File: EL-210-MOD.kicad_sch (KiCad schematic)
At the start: 2 parts, among them P1 EL-210-KEY, U1 9-ST-20

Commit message: Rough layout of the digital part.
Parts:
- added U2: STM32G0B1KET6, Package_QFP:LQFP-32_7x7mm_P0.8mm, symbol STM32G0B1KET6:STM32G0B1KET6
- added U3: MAX6934AQH+D, Package_LCC:PLCC-44, symbol MAX6934A:MAX6934AQH+D
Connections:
- net +3V3: now also U2.4 (VDD/VDDA)
- net GND: now also U2.5 (VSS/VSSA), U3.22 (GND)
- net KD3: now reaches P1.10 (D3)
- net KD3: now also U2.10 (PA3)
- net KD2: now reaches P1.11 (D2)
- net KD2: now also U2.9 (PA2)
- net KD1: now reaches P1.13 (D1)
- net KD1: now also U2.8 (PA1)
- net KD0: now reaches P1.14 (D0)
- net KD0: now also U2.7 (PA0)
- net KEY1: now reaches P1.2 (KEY1)
- net KEY1: now also U2.21 (PA10)
- net KEY2: now reaches P1.3 (KEY2)
- net KEY2: now also U2.20 (PC6)
- net KEY3: now reaches P1.4 (KEY3)
- net KEY3: now also U2.17 (PB2)
- net KD8: now reaches P1.5 (D8)
- net KD8: now also U2.16 (PB1)
- net KD7: now reaches P1.6 (D7)
- net KD7: now also U2.15 (PB0)
- net KD6: now reaches P1.7 (D6)
- net KD6: now also U2.13 (PA6)
- net KD5: now reaches P1.8 (D5)
- net KD5: now also U2.12 (PA5)
- net KD4: now reaches P1.9 (D4)
- net KD4: now also U2.11 (PA4)
- net H1: now reaches U1.1 (H1)
- net at U1.10 (D4): now also U3.34 (OUT8)
- net at U1.11 (Seg_d): now also U3.35 (OUT7)
- net at U1.12 (D3): now also U3.36 (OUT6)
- net at U1.13 (DP): now also U3.37 (OUT5)
- net at U1.14 (D2): now also U3.38 (OUT4)
- net at U1.15 (Seg_c): now also U3.39 (OUT3)
- net at U1.16 (D1): now also U3.40 (OUT2)
- net at U1.17 (Seg_b): now also U3.41 (OUT1)
- net at U1.18 (D0): now also U3.42 (OUT0)
- net H2: now reaches U1.19 (H2)
- net SEG_A: now reaches U1.2 (Seg_a)
- net SEG_A: now also U3.20 (OUT16)
- net at U1.3 (D8): now also U3.25 (OUT15)
- net at U1.4 (Seg_g): now also U3.26 (OUT14)
- net at U1.5 (D7): now also U3.27 (OUT13)
- net at U1.6 (Seg_f): now also U3.30 (OUT12)
- net at U1.7 (D6): now also U3.31 (OUT11)
- net at U1.8 (Seg_e): now also U3.32 (OUT10)
- net at U1.9 (D5): now also U3.33 (OUT9)
- new net BLANK: U2.23 (PA12_PA10), U3.21 (BLANK)
- new net EN24V: U2.32 (PB8)
- new net LOAD: U2.22 (PA11_PA9), U3.24 (LOAD)
- new net LPUART2_RX: U2.31 (PB7)
- new net LPUART2_TX: U2.30 (PB6)
- new net NRST: U2.6 (PF2-NRST)
- new net SPI1_MOSI: U2.29 (PB5), U3.43 (DIN)
- new net SPI1_SCK: U2.27 (PB3), U3.23 (CLK)
- new net SWCLK: U2.25 (PA14-BOOT0)
- new net SWDIO: U2.24 (PA13)
- new net TIM1_CH1: U2.18 (PA8)
- new net TIM1_CH1N: U2.14 (PA7)
- new net TIM2_CH2: U2.19 (PA9)
- no-connect marks 0 -> 22
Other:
- moved on the sheet: P1, U1

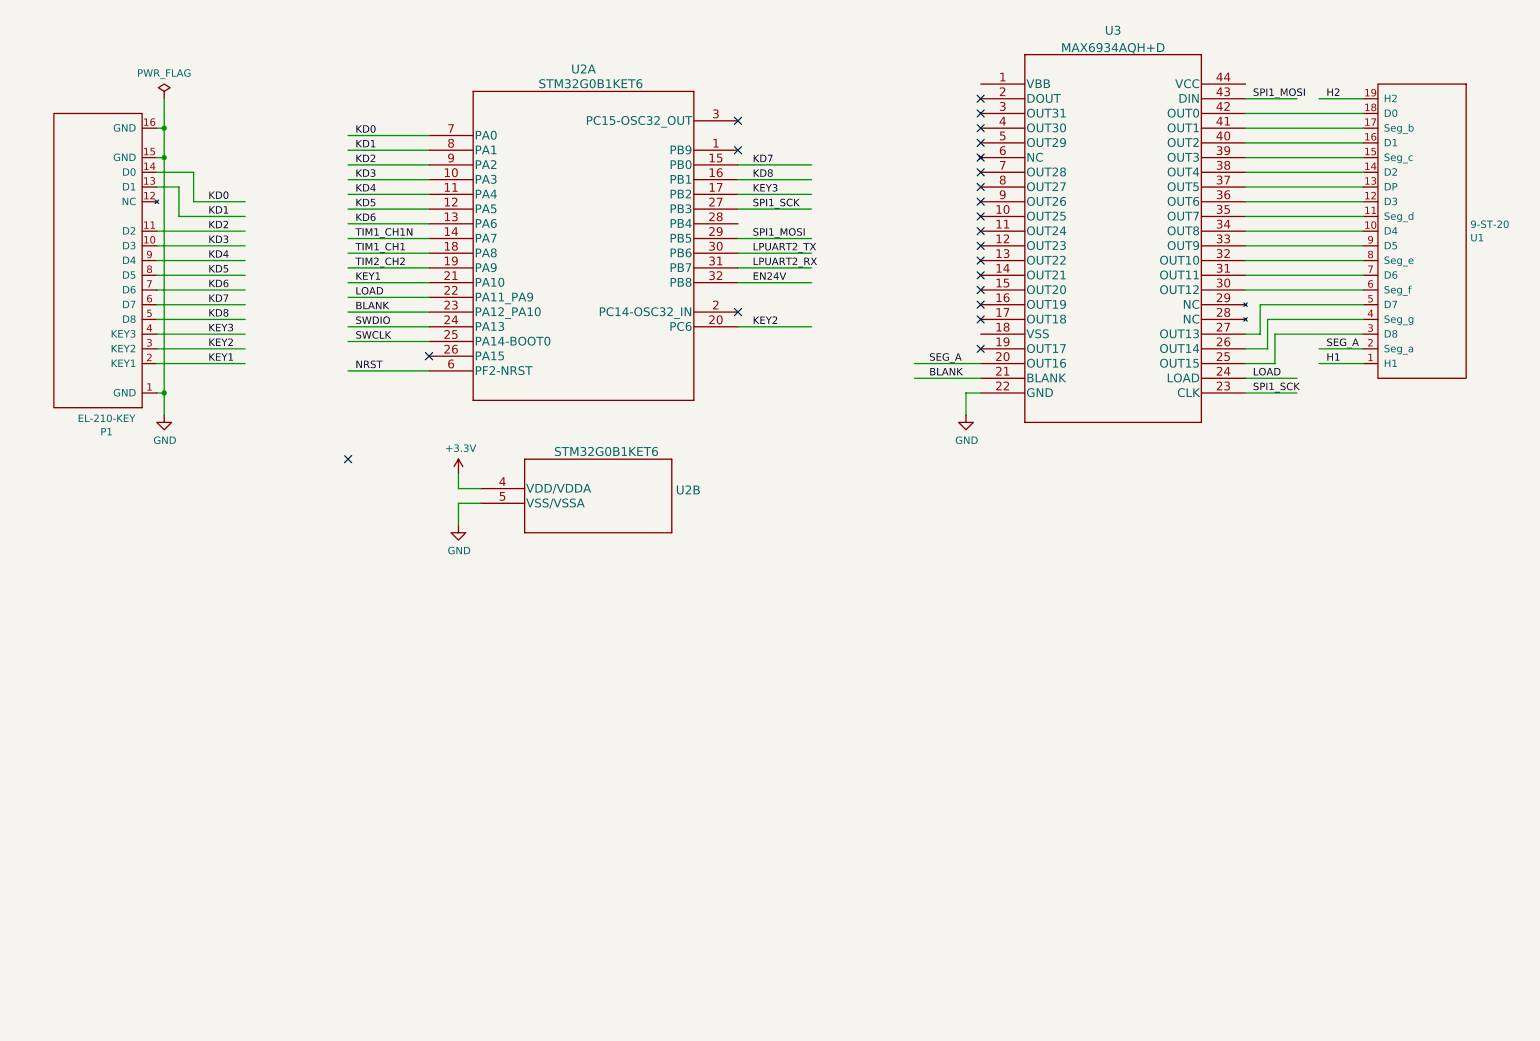
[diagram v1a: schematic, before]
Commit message: Add analog parts.
Waiting for SWD port.
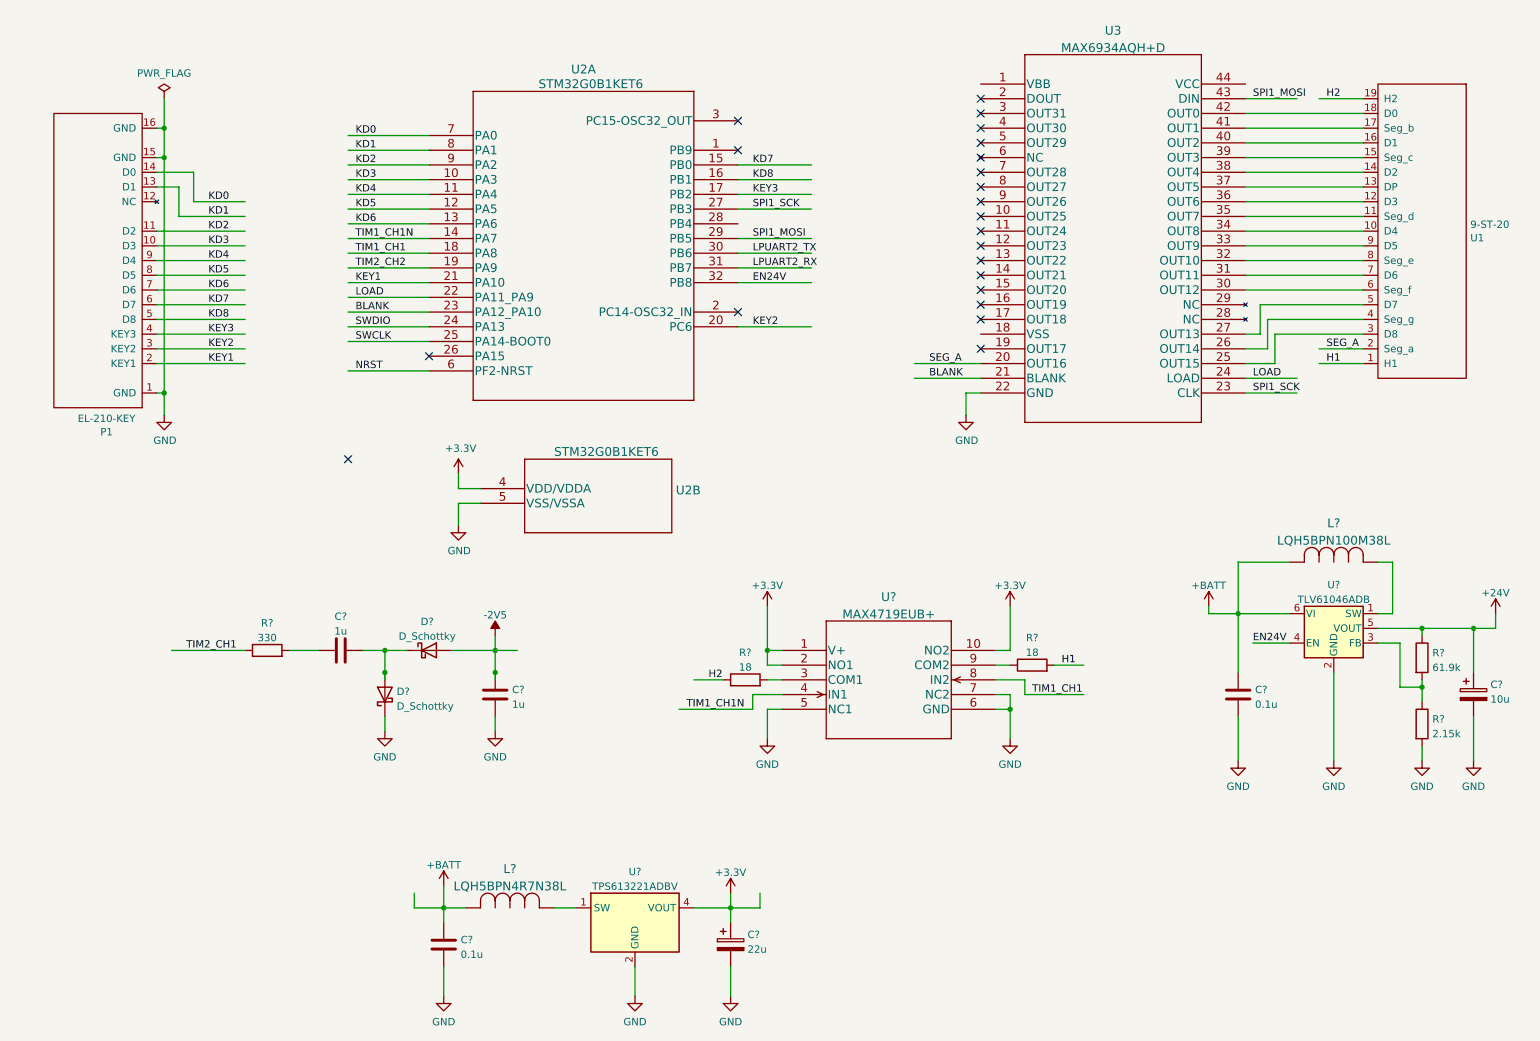
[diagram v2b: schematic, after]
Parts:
- added C? (x2): 0.1u, symbol Device:C
- added C? (x2): 1u, symbol Device:C
- added C?: 10u, symbol Device:C_Polarized
- added C?: 22u, symbol Device:C_Polarized
- added D? (x2): D_Schottky, symbol Device:D_Schottky
- added L?: LQH5BPN4R7N38L, IND_LQH5BPN_MUR, symbol LQH5BPN100M38L:LQH5BPN100M38L
- added L?: LQH5BPN100M38L, IND_LQH5BPN_MUR, symbol LQH5BPN100M38L:LQH5BPN100M38L
- added R?: 2.15k, symbol Device:R
- added R?: 330, symbol Device:R
- added R? (x2): 18, symbol Device:R
- added R?: 61.9k, symbol Device:R
- added U?: TPS613221ADBV, Package_TO_SOT_SMD:SOT-23-5, symbol Regulator_Switching:TPS613221ADBV
- added U?: TLV61046ADB, Package_TO_SOT_SMD:SOT-23-6, symbol Regulator_Switching:TLV61046ADB
- added U?: MAX4719EUB+, 21-0061L, symbol MAX4719E:MAX4719EUB+
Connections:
- net +3V3: now also C?.1, U?.1 (V+), U?.10 (NO2), U?.2 (NO1), U?.4 (VOUT)
- net EN24V: now also U?.4 (EN)
- net GND: now also C?.2, C?.2, C?.2, C?.2, C?.2, D?.1 (K), R?.2, U?.2 (GND), U?.2 (GND), U?.5 (NC1), U?.6 (GND), U?.7 (NC2)
- net H1: now also R?.2
- net H2: now also R?.1
- net TIM1_CH1: now also U?.8 (IN2)
- net TIM1_CH1N: now also U?.4 (IN1)
- new net: C?.1, R?.2
- new net: C?.2, D?.1 (K), D?.2 (A)
- new net: R?.1, R?.2, U?.3 (FB)
- new net: L?.1, U?.1 (SW) (x2)
- new net: R?.2, U?.3 (COM1)
- new net: R?.1, U?.9 (COM2)
- new net +24V: C?.1, R?.1, U?.5 (VOUT)
- new net +BATT: C?.1, C?.1, L?.2, L?.2, U?.6 (VI)
- new net -2V5: C?.1, D?.2 (A)
- new net TIM2_CH1: R?.1

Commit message: Schematics is finished.
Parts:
- added C10, C2, C3, C7, C8: C, Capacitor_SMD:C_0603_1608Metric_Pad1.08x0.95mm_HandSolder, symbol Device:C
- added J1: Conn_01x05, Connector_PinHeader_2.54mm:PinHeader_1x05_P2.54mm_Horizontal, symbol Connector_Generic:Conn_01x05
- C1, C4, C5, C9: renamed from C?; footprint (none) -> Capacitor_SMD:C_0603_1608Metric_Pad1.08x0.95mm_HandSolder
- C11: renamed from C?; value 10u -> UZG1H100MCL1GB; footprint (none) -> Capacitor_SMD:CP_Elec_4x3.9
- C6: renamed from C?; value 22u -> UZG0J220MCL1GB; footprint (none) -> Capacitor_SMD:CP_Elec_6.3x3.9
- D1, D2: renamed from D?; footprint (none) -> Diode_SMD:D_0603_1608Metric_Pad1.05x0.95mm_HandSolder
- L1, L2: renamed from L?; footprint IND_LQH5BPN_MUR -> project_lib:LQH5BPN100M38L
- R1, R2, R3, R4, R5: renamed from R?; footprint (none) -> Resistor_SMD:R_0603_1608Metric_Pad0.98x0.95mm_HandSolder
- U5: renamed from U?; footprint 21-0061L -> Package_SO:MSOP-10_3x3mm_P0.5mm
- gave numbers to parts that had none: 2
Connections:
- net LPUART2_RX is gone; now on net LPUART2_TX: U2.31 (PB7)
- net +24V: now also U3.1 (VBB), C8.1
- net +3V3: now also U3.44 (VCC), C10.1, C3.2
- net -2V5: now also U3.18 (VSS), C7.1
- net GND: now also C10.2, C2.2, C3.1, C7.2, C8.2, J1.2 (Pin_2)
- net LPUART2_TX: now also J1.5 (Pin_5)
- net NRST: now also C2.1, J1.4 (Pin_4)
- net SWCLK: now also J1.1 (Pin_1)
- net SWDIO: now also J1.3 (Pin_3)
- no-connect marks 22 -> 21
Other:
- note added: "RX"
- moved on the sheet: C1, C11, C5, C9, D1, D2, L2, R1, R2, R3, R4, R5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

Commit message: Change PLCC footprint to handsolder type
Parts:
- U3: footprint Package_LCC:PLCC-44 -> plcc44_hs:PLCC44_handsoldering
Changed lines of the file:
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@@
       (effects (font (size 1.524 1.524)))
     )
-    (property "Footprint" "Package_LCC:PLCC-44" (id 2) (at 210.82 29.464 0)
+    (property "Footprint" "plcc44_hs:PLCC44_handsoldering" (id 2) (at 210.82 29.464 0)
       (effects (font (size 1.524 1.524)) hide)
     )
@@
     )
     (path "/4099be24-4041-44aa-b3ae-1d400eb2ae96"
-      (reference "U3") (unit 1) (value "MAX6934AQH+D") (footprint "Package_LCC:PLCC-44")
+      (reference "U3") (unit 1) (value "MAX6934AQH+D") (footprint "plcc44_hs:PLCC44_handsoldering")
     )
     (path "/4aae5fbc-1e32-4cd8-9d8d-92887dc880d2"

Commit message: parts placed.
The version number is written.
The SMD pad of the Ls are modifed.
Routing is not finished.
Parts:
- added J2: Conn_01x02, Connector_PinHeader_2.54mm:PinHeader_1x02_P2.54mm_Vertical, symbol Connector_Generic:Conn_01x02
- C10, C2, C3, C7, C8: value C -> 0.1u
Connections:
- net TIM2_CH2 is gone; now on net TIM2_CH1: U2.19 (PA9)
- net +BATT: now also J2.1 (Pin_1)
- net GND: now also J2.2 (Pin_2)
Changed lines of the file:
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@@
+    (stroke (width 0) (type default) (color 0 0 0 0))
+  )
+  (wire (pts (xy 25.4 143.51) (xy 24.13 143.51))
     (stroke (width 0) (type default) (color 0 0 0 0))
   )
@@
     (stroke (width 0) (type default) (color 0 0 0 0))
   )
+  (wire (pts (xy 25.4 140.97) (xy 24.13 140.97))
+    (stroke (width 0) (type default) (color 0 0 0 0))
+  )
   (wire (pts (xy 173.99 135.89) (xy 179.07 135.89))
     (stroke (width 0) (type default) (color 0 0 0 0))
@@
     (stroke (width 0) (type default) (color 0 0 0 0))
   )
+  (wire (pts (xy 24.13 143.51) (xy 24.13 144.78))
+    (stroke (width 0) (type default) (color 0 0 0 0))
+  )
   (wire (pts (xy 78.74 71.12) (xy 92.71 71.12))
     (stroke (width 0) (type default) (color 0 0 0 0))
@@
     (stroke (width 0) (type default) (color 0 0 0 0))
   )
+  (wire (pts (xy 24.13 140.97) (xy 24.13 138.43))
+    (stroke (width 0) (type default) (color 0 0 0 0))
+  )
   (wire (pts (xy 46.99 36.83) (xy 46.99 31.75))
     (stroke (width 0) (type default) (color 0 0 0 0))
@@
     (effects (font (size 1.27 1.27)) (justify left bottom))
   )
-  (label "TIM2_CH2" (at 80.01 60.96 0)
+  (label "TIM2_CH1" (at 80.01 60.96 0)
     (effects (font (size 1.27 1.27)) (justify left bottom))
   )
@@
       (effects (font (size 1.27 1.27)) (justify left))
     )
-    (property "Value" "C" (id 1) (at 84.201 85.5222 0)
-      (effects (font (size 1.27 1.27)) (justify left))
+    (property "Value" "0.1u" (id 1) (at 84.201 85.5222 0)
+      (effects (font (size 1.27 1.27)) (justify left) hide)
     )
     (property "Footprint" "Capacitor_SMD:C_0603_1608Metric_Pad1.08x0.95mm_HandSolder" (id 2) (at 82.2452 87.63 0)
@@
       (effects (font (size 1.27 1.27)) (justify right))
     )
-    (property "Value" "C" (id 1) (at 94.361 102.0322 0)
+    (property "Value" "0.1u" (id 1) (at 94.361 102.0322 0)
       (effects (font (size 1.27 1.27)) (justify right))
     )
@@
     (pin "6")
   )
+  (symbol (lib_id "power:GND") (at 24.13 144.78 0) (unit 1)
+    (in_bom yes) (on_board yes) (fields_autoplaced)
+    (property "Reference" "#PWR0101" (id 0) (at 24.13 151.13 0)
+      (effects (font (size 1.27 1.27)) hide)
+    )
+    (property "Value" "GND" (id 1) (at 24.13 149.2234 0))
+    (property "Footprint" "" (id 2) (at 24.13 144.78 0)
+      (effects (font (size 1.27 1.27)) hide)
+    )
+    (property "Datasheet" "" (id 3) (at 24.13 144.78 0)
+      (effects (font (size 1.27 1.27)) hide)
+    )
+    (pin "1")
+  )
   (symbol (lib_id "power:-2V5") (at 182.88 60.96 0) (unit 1)
     (in_bom yes) (on_board yes) (fields_autoplaced)
@@
     (pin "1")
   )
+  (symbol (lib_id "power:+BATT") (at 24.13 138.43 0) (unit 1)
+    (in_bom yes) (on_board yes) (fields_autoplaced)
+    (property "Reference" "#PWR0102" (id 0) (at 24.13 142.24 0)
+      (effects (font (size 1.27 1.27)) hide)
+    )
+    (property "Value" "+BATT" (id 1) (at 24.13 134.8542 0))
+    (property "Footprint" "" (id 2) (at 24.13 138.43 0)
+      (effects (font (size 1.27 1.27)) hide)
+    )
+    (property "Datasheet" "" (id 3) (at 24.13 138.43 0)
+      (effects (font (size 1.27 1.27)) hide)
+    )
+    (pin "1")
+  )
   (symbol (lib_id "power:-2V5") (at 100.33 128.27 0) (unit 1)
     (in_bom yes) (on_board yes) (fields_autoplaced)
@@
     )
     (pin "1")
+  )
+  (symbol (lib_id "Connector_Generic:Conn_01x02") (at 30.48 140.97 0) (unit 1)
+    (in_bom yes) (on_board yes) (fields_autoplaced)
+    (property "Reference" "J2" (id 0) (at 32.512 141.4053 0)
+      (effects (font (size 1.27 1.27)) (justify left))
+    )
+    (property "Value" "Conn_01x02" (id 1) (at 32.512 143.9422 0)
+      (effects (font (size 1.27 1.27)) (justify left))
+    )
+    (property "Footprint" "Connector_PinHeader_2.54mm:PinHeader_1x02_P2.54mm_Vertical" (id 2) (at 30.48 140.97 0)
+      (effects (font (size 1.27 1.27)) hide)
+    )
+    (property "Datasheet" "~" (id 3) (at 30.48 140.97 0)
+      (effects (font (size 1.27 1.27)) hide)
+    )
+    (pin "1")
+    (pin "2")
   )
   (symbol (lib_id "power:PWR_FLAG") (at 237.49 116.84 0) (unit 1)
@@
       (effects (font (size 1.27 1.27)) (justify left))
     )
-    (property "Value" "C" (id 1) (at 244.221 28.3722 0)
+    (property "Value" "0.1u" (id 1) (at 244.221 28.3722 0)
       (effects (font (size 1.27 1.27)) (justify left))
     )
@@
       (effects (font (size 1.27 1.27)) (justify left))
     )
-    (property "Value" "C" (id 1) (at 183.261 43.6122 0)
+    (property "Value" "0.1u" (id 1) (at 183.261 43.6122 0)
       (effects (font (size 1.27 1.27)) (justify left))
     )
@@
       (effects (font (size 1.27 1.27)) (justify left))
     )
-    (property "Value" "C" (id 1) (at 179.451 72.8222 0)
+    (property "Value" "0.1u" (id 1) (at 179.451 72.8222 0)
       (effects (font (size 1.27 1.27)) (justify left))
     )
@@
       (reference "#PWR029") (unit 1) (value "+24V") (footprint "")
     )
+    (path "/68a7fe44-fe87-4a41-a736-4864b42058d6"
+      (reference "#PWR0101") (unit 1) (value "GND") (footprint "")
+    )
+    (path "/84c6f55b-23ee-495d-a57e-d8f651aa7b0a"
+      (reference "#PWR0102") (unit 1) (value "+BATT") (footprint "")
+    )
     (path "/11a5cd1c-f2c6-4399-8a5b-503c01f732fd"
       (reference "C1") (unit 1) (value "1u") (footprint "Capacitor_SMD:C_0603_1608Metric_Pad1.08x0.95mm_HandSolder")
     )
     (path "/454b7eee-711e-4660-bc2d-698650647b90"
-      (reference "C2") (unit 1) (value "C") (footprint "Capacitor_SMD:C_0603_1608Metric_Pad1.08x0.95mm_HandSolder")
+      (reference "C2") (unit 1) (value "0.1u") (footprint "Capacitor_SMD:C_0603_1608Metric_Pad1.08x0.95mm_HandSolder")
     )
     (path "/540b2c1d-0ace-48b1-b85d-c14884aee95e"
-      (reference "C3") (unit 1) (value "C") (footprint "Capacitor_SMD:C_0603_1608Metric_Pad1.08x0.95mm_HandSolder")
+      (reference "C3") (unit 1) (value "0.1u") (footprint "Capacitor_SMD:C_0603_1608Metric_Pad1.08x0.95mm_HandSolder")
     )
     (path "/0da27400-59b7-4679-90c2-1eb0b49f39e8"
@@
     )
     (path "/f5b00abc-a391-4427-9c9b-fa38c85349fd"
-      (reference "C7") (unit 1) (value "C") (footprint "Capacitor_SMD:C_0603_1608Metric_Pad1.08x0.95mm_HandSolder")
+      (reference "C7") (unit 1) (value "0.1u") (footprint "Capacitor_SMD:C_0603_1608Metric_Pad1.08x0.95mm_HandSolder")
     )
     (path "/c4cd7ce8-a0ea-4257-8202-42407e94a576"
-      (reference "C8") (unit 1) (value "C") (footprint "Capacitor_SMD:C_0603_1608Metric_Pad1.08x0.95mm_HandSolder")
+      (reference "C8") (unit 1) (value "0.1u") (footprint "Capacitor_SMD:C_0603_1608Metric_Pad1.08x0.95mm_HandSolder")
     )
     (path "/802cac39-7394-4c88-b703-788a476bdc86"
@@
     )
     (path "/af9fafaa-9a18-43f4-8eb4-120ac0f931ad"
-      (reference "C10") (unit 1) (value "C") (footprint "Capacitor_SMD:C_0603_1608Metric_Pad1.08x0.95mm_HandSolder")
+      (reference "C10") (unit 1) (value "0.1u") (footprint "Capacitor_SMD:C_0603_1608Metric_Pad1.08x0.95mm_HandSolder")
     )
     (path "/2fdd038b-8927-431e-9c67-f8f1c25fc8d5"
@@
       (reference "J1") (unit 1) (value "Conn_01x05") (footprint "Connector_PinHeader_2.54mm:PinHeader_1x05_P2.54mm_Horizontal")
     )
+    (path "/8ba71748-cbbe-4e0e-a7ec-39fda6a3092a"
+      (reference "J2") (unit 1) (value "Conn_01x02") (footprint "Connector_PinHeader_2.54mm:PinHeader_1x02_P2.54mm_Vertical")
+    )
     (path "/c8ef8ae9-b11b-4ab4-b66d-011626d539e6"
